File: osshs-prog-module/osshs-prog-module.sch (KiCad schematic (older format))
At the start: 11 parts, among them J1 Conn_02x03_Odd_Even, SW1 SW_Push, U1 STM32F103RETx

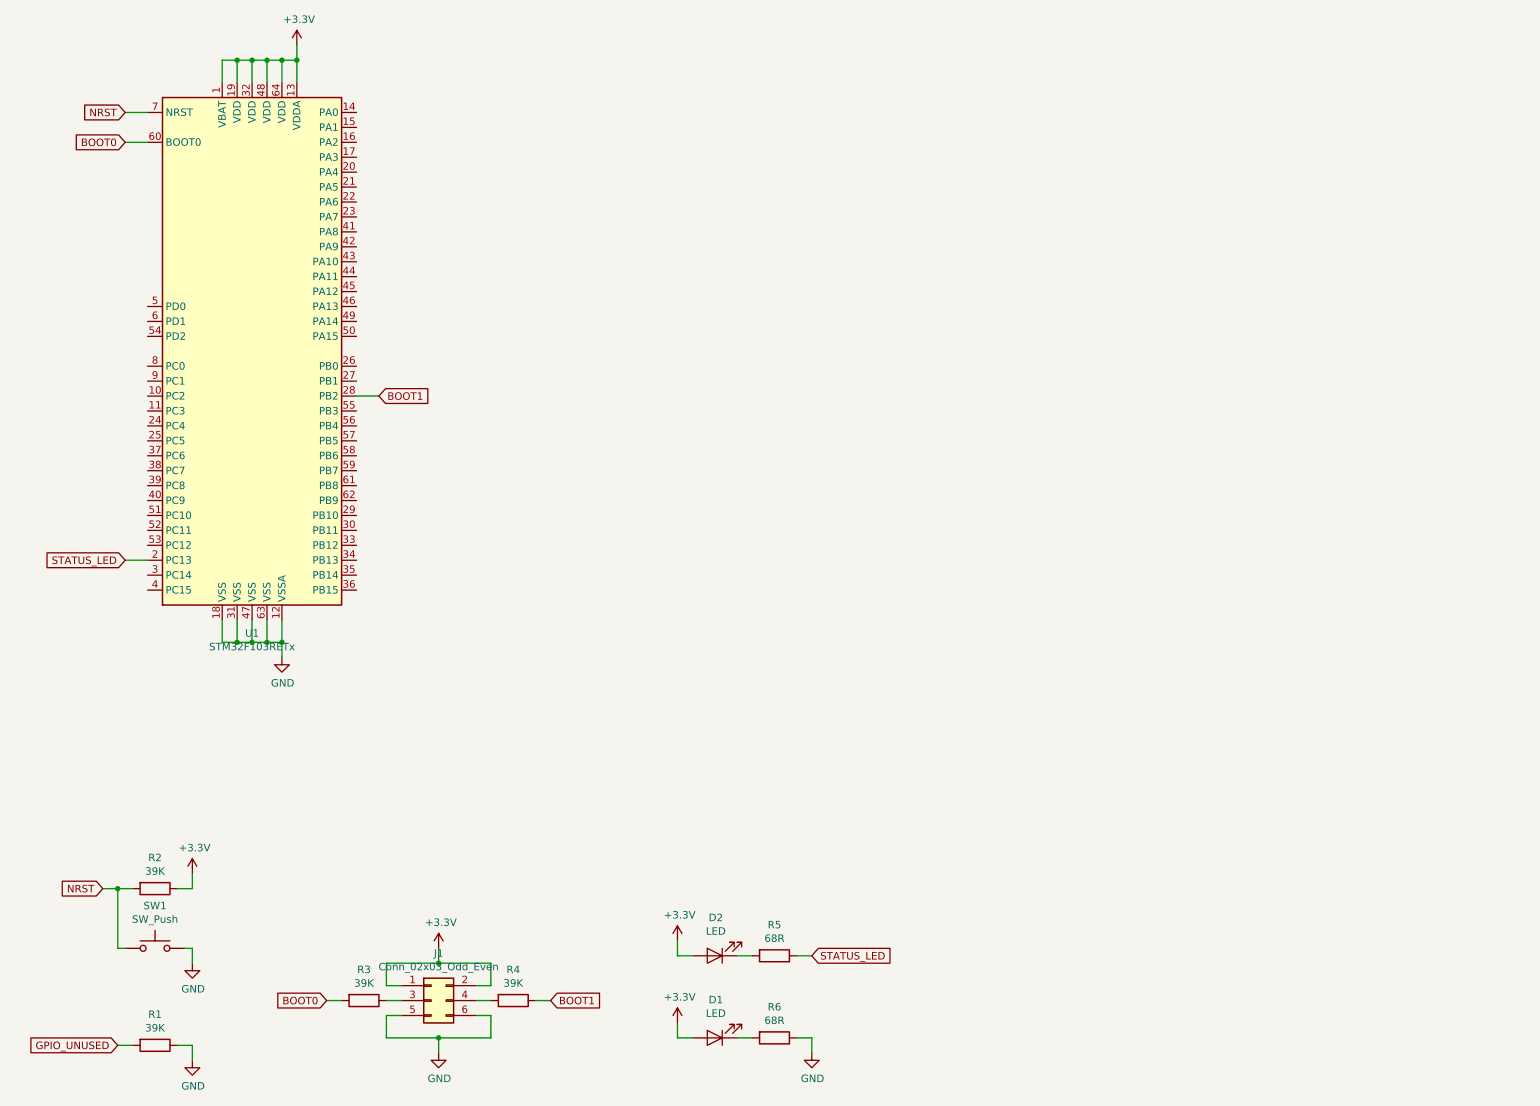
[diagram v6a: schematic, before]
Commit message: Add SWD connector
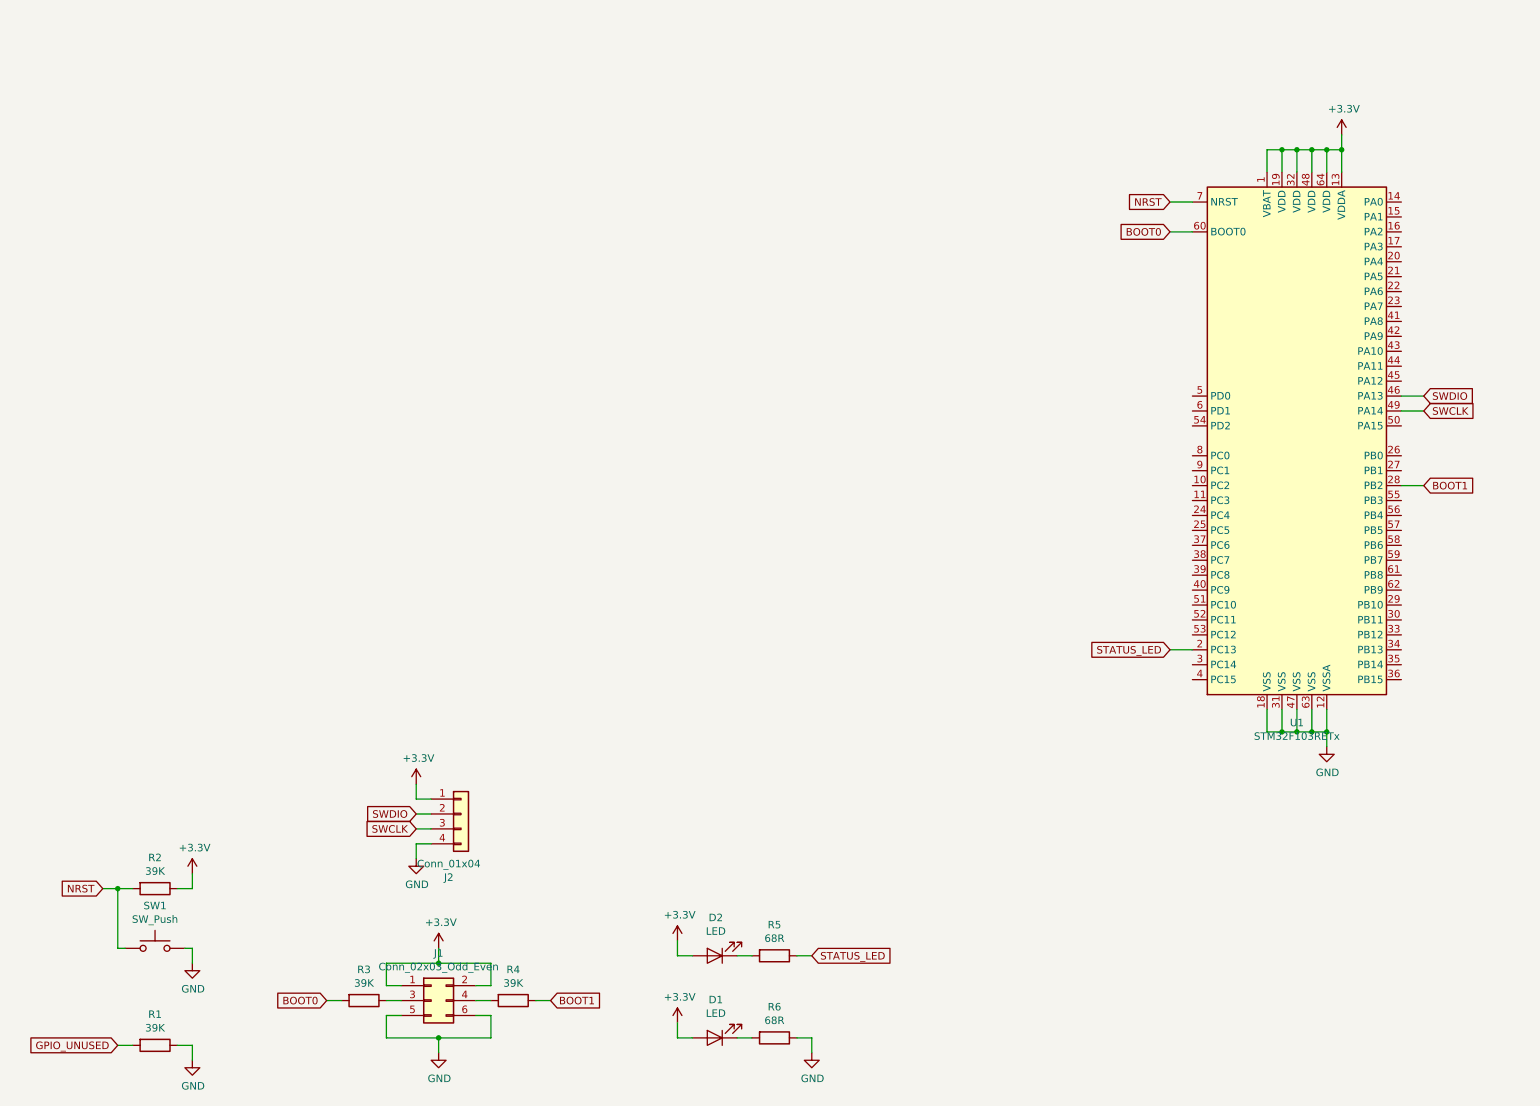
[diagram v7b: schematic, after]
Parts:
- added J2: Conn_01x04, Connector_PinHeader_2.54mm:PinHeader_1x04_P2.54mm_Vertical, symbol Connector_Generic:Conn_01x04
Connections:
- net +3V3: now also J2.1 (Pin_1)
- net GND: now also J2.4 (Pin_4)
- net SWDIO: now reaches U1.46 (PA13)
- net SWDIO: now also J2.2 (Pin_2)
- net SWCLK: now reaches U1.49 (PA14)
- net SWCLK: now also J2.3 (Pin_3)
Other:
- moved on the sheet: U1
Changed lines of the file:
@@
 L MCU_ST_STM32F1:STM32F103RETx U1
 U 1 1 5DE66C62
-P 2000 2800
-F 0 "U1" H 2000 911 50  0000 C CNN
-F 1 "STM32F103RETx" H 2000 820 50  0000 C CNN
-F 2 "Package_QFP:LQFP-64_10x10mm_P0.5mm" H 1400 1100 50  0001 R CNN
-F 3 "http://www.st.com/st-web-ui/static/active/en/resource/technical/document/datasheet/CD00191185.pdf" H 2000 2800 50  0001 C CNN
-	1    2000 2800
-	1    0    0    -1
-$EndComp
-Wire Wire Line
-	1300 1200 1150 1200
-Wire Wire Line
-	1300 1400 1150 1400
-Wire Wire Line
-	1300 4200 1150 4200
-Wire Wire Line
-	1800 4600 1800 4750
-Wire Wire Line
-	1900 4600 1900 4750
-Wire Wire Line
-	2000 4600 2000 4750
-Wire Wire Line
-	2100 4600 2100 4750
-Wire Wire Line
-	2200 4600 2200 4750
-Wire Wire Line
-	2700 3100 2850 3100
-Wire Wire Line
-	2300 1000 2300 850
-Wire Wire Line
-	2200 1000 2200 850
-Wire Wire Line
-	2100 1000 2100 850
-Wire Wire Line
-	2000 1000 2000 850
-Wire Wire Line
-	1900 1000 1900 850
-Wire Wire Line
-	1800 1000 1800 850
-Text GLabel 2850 3100 2    50   Input ~ 0
+P 9000 3400
+F 0 "U1" H 9000 1511 50  0000 C CNN
+F 1 "STM32F103RETx" H 9000 1420 50  0000 C CNN
+F 2 "Package_QFP:LQFP-64_10x10mm_P0.5mm" H 8400 1700 50  0001 R CNN
+F 3 "http://www.st.com/st-web-ui/static/active/en/resource/technical/document/datasheet/CD00191185.pdf" H 9000 3400 50  0001 C CNN
+	1    9000 3400
+	1    0    0    -1
+$EndComp
+Wire Wire Line
+	8300 1800 8150 1800
+Wire Wire Line
+	8300 2000 8150 2000
+Wire Wire Line
+	8300 4800 8150 4800
+Wire Wire Line
+	8800 5200 8800 5350
+Wire Wire Line
+	8900 5200 8900 5350
+Wire Wire Line
+	9000 5200 9000 5350
+Wire Wire Line
+	9100 5200 9100 5350
+Wire Wire Line
+	9200 5200 9200 5350
+Wire Wire Line
+	9700 3700 9850 3700
+Wire Wire Line
+	9300 1600 9300 1450
+Wire Wire Line
+	9200 1600 9200 1450
+Wire Wire Line
+	9100 1600 9100 1450
+Wire Wire Line
+	9000 1600 9000 1450
+Wire Wire Line
+	8900 1600 8900 1450
+Wire Wire Line
+	8800 1600 8800 1450
+Text GLabel 9850 3700 2    50   Input ~ 0
 BOOT1
-Text GLabel 1150 4200 0    50   Input ~ 0
+Text GLabel 8150 4800 0    50   Input ~ 0
 STATUS_LED
 Text GLabel 1100 7450 0    50   Input ~ 0
@@
 Wire Wire Line
 	1500 7450 1600 7450
-Text GLabel 1150 1200 0    50   Input ~ 0
+Text GLabel 8150 1800 0    50   Input ~ 0
 NRST
 Text GLabel 1000 6400 0    50   Input ~ 0
@@
 $EndComp
 Wire Wire Line
-	1800 850  1900 850
-Wire Wire Line
-	1900 850  2000 850
-Connection ~ 1900 850
-Wire Wire Line
-	2000 850  2100 850
-Connection ~ 2000 850
-Wire Wire Line
-	2100 850  2200 850
-Connection ~ 2100 850
-Wire Wire Line
-	2200 850  2300 850
-Connection ~ 2200 850
-Wire Wire Line
-	2300 850  2300 750
-Connection ~ 2300 850
+	8800 1450 8900 1450
+Wire Wire Line
+	8900 1450 9000 1450
+Connection ~ 8900 1450
+Wire Wire Line
+	9000 1450 9100 1450
+Connection ~ 9000 1450
+Wire Wire Line
+	9100 1450 9200 1450
+Connection ~ 9100 1450
+Wire Wire Line
+	9200 1450 9300 1450
+Connection ~ 9200 1450
+Wire Wire Line
+	9300 1450 9300 1350
+Connection ~ 9300 1450
 $Comp
 L power:+3.3V #PWR0104
 U 1 1 5DEAFF7F
-P 2300 750
-F 0 "#PWR0104" H 2300 600 50  0001 C CNN
-F 1 "+3.3V" H 2315 923 50  0000 C CNN
-F 2 "" H 2300 750 50  0001 C CNN
-F 3 "" H 2300 750 50  0001 C CNN
-	1    2300 750
-	1    0    0    -1
-$EndComp
-Wire Wire Line
-	1800 4750 1900 4750
-Wire Wire Line
-	2000 4750 1900 4750
-Connection ~ 1900 4750
-Wire Wire Line
-	2000 4750 2100 4750
-Connection ~ 2000 4750
-Connection ~ 2100 4750
-Wire Wire Line
-	2100 4750 2200 4750
-Wire Wire Line
-	2200 4750 2200 4850
-Connection ~ 2200 4750
+P 9300 1350
+F 0 "#PWR0104" H 9300 1200 50  0001 C CNN
+F 1 "+3.3V" H 9315 1523 50  0000 C CNN
+F 2 "" H 9300 1350 50  0001 C CNN
+F 3 "" H 9300 1350 50  0001 C CNN
+	1    9300 1350
+	1    0    0    -1
+$EndComp
+Wire Wire Line
+	8800 5350 8900 5350
+Wire Wire Line
+	9000 5350 8900 5350
+Connection ~ 8900 5350
+Wire Wire Line
+	9000 5350 9100 5350
+Connection ~ 9000 5350
+Connection ~ 9100 5350
+Wire Wire Line
+	9100 5350 9200 5350
+Wire Wire Line
+	9200 5350 9200 5450
+Connection ~ 9200 5350
 $Comp
 L power:GND #PWR0105
 U 1 1 5DEBBFB0
-P 2200 4850
-F 0 "#PWR0105" H 2200 4600 50  0001 C CNN
-F 1 "GND" H 2205 4677 50  0000 C CNN
-F 2 "" H 2200 4850 50  0001 C CNN
-F 3 "" H 2200 4850 50  0001 C CNN
-	1    2200 4850
-	1    0    0    -1
-$EndComp
-Text GLabel 1150 1400 0    50   Input ~ 0
+P 9200 5450
+F 0 "#PWR0105" H 9200 5200 50  0001 C CNN
+F 1 "GND" H 9205 5277 50  0000 C CNN
+F 2 "" H 9200 5450 50  0001 C CNN
+F 3 "" H 9200 5450 50  0001 C CNN
+	1    9200 5450
+	1    0    0    -1
+$EndComp
+Text GLabel 8150 2000 0    50   Input ~ 0
 BOOT0
 $Comp
@@
 Wire Wire Line
 	5650 7400 5750 7400
+$Comp
+L Connector_Generic:Conn_01x04 J2
+U 1 1 5E1095F9
+P 3400 5900
+F 0 "J2" H 3318 5475 50  0000 C CNN
+F 1 "Conn_01x04" H 3318 5566 50  0000 C CNN
+F 2 "Connector_PinHeader_2.54mm:PinHeader_1x04_P2.54mm_Vertical" H 3400 5900 50  0001 C CNN
+F 3 "~" H 3400 5900 50  0001 C CNN
+	1    3400 5900
+	1    0    0    -1
+$EndComp
+$Comp
+L power:+3.3V #PWR0111
+U 1 1 5E13D211
+P 3100 5700
+F 0 "#PWR0111" H 3100 5550 50  0001 C CNN
+F 1 "+3.3V" H 3115 5873 50  0000 C CNN
+F 2 "" H 3100 5700 50  0001 C CNN
+F 3 "" H 3100 5700 50  0001 C CNN
+	1    3100 5700
+	1    0    0    -1
+$EndComp
+Wire Wire Line
+	3100 5700 3100 5800
+Wire Wire Line
+	3100 5800 3200 5800
+Wire Wire Line
+	3200 6100 3100 6100
+Wire Wire Line
+	3100 6100 3100 6200
+$Comp
+L power:GND #PWR0112
+U 1 1 5E141D1C
+P 3100 6200
+F 0 "#PWR0112" H 3100 5950 50  0001 C CNN
+F 1 "GND" H 3105 6027 50  0000 C CNN
+F 2 "" H 3100 6200 50  0001 C CNN
+F 3 "" H 3100 6200 50  0001 C CNN
+	1    3100 6200
+	1    0    0    -1
+$EndComp
+Wire Wire Line
+	3100 5900 3200 5900
+Wire Wire Line
+	3100 6000 3200 6000
+Text GLabel 3100 5900 0    50   Input ~ 0
+SWDIO
+Text GLabel 3100 6000 0    50   Input ~ 0
+SWCLK
+Text GLabel 9850 3100 2    50   Input ~ 0
+SWDIO
+Wire Wire Line
+	9700 3100 9850 3100
+Wire Wire Line
+	9700 3200 9850 3200
+Text GLabel 9850 3200 2    50   Input ~ 0
+SWCLK
 $EndSCHEMATC

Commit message: Add debug USART connector
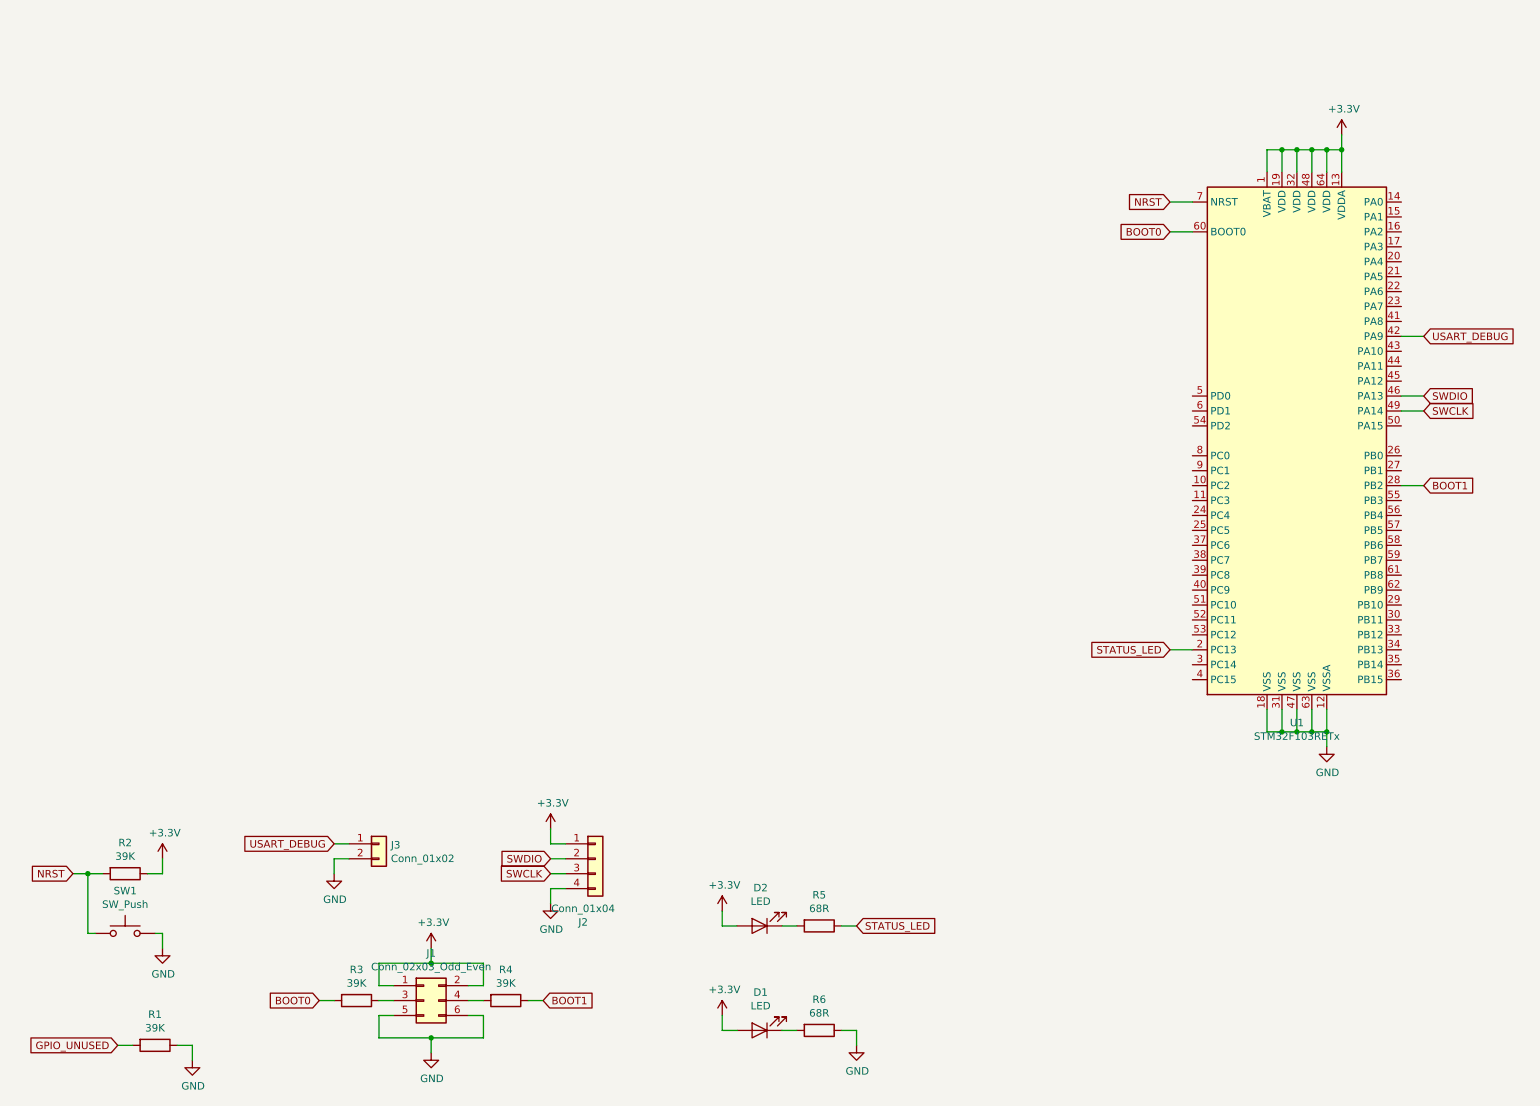
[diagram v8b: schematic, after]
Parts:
- added J3: Conn_01x02, symbol Connector_Generic:Conn_01x02
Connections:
- net GND: now also J3.2 (Pin_2)
- net USART_DEBUG: now reaches U1.42 (PA9)
- net USART_DEBUG: now also J3.1 (Pin_1)
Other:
- moved on the sheet: D1, D2, J1, J2, R2, R3, R4, R5, R6, SW1
